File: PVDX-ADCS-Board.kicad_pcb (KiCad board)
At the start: 2 copper layers, 82.5 x 82.5 mm, 0 parts

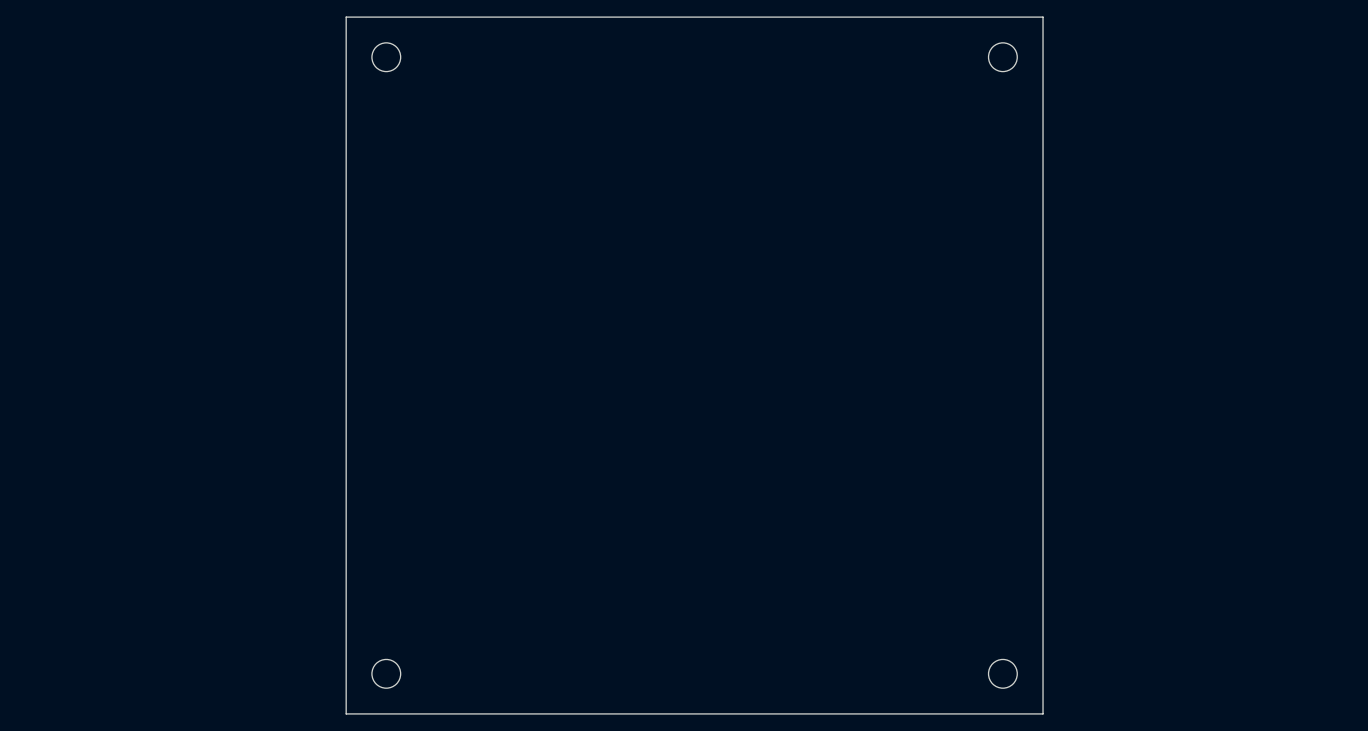
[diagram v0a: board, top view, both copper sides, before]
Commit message: routed PMB subcircuit, assigned eda models
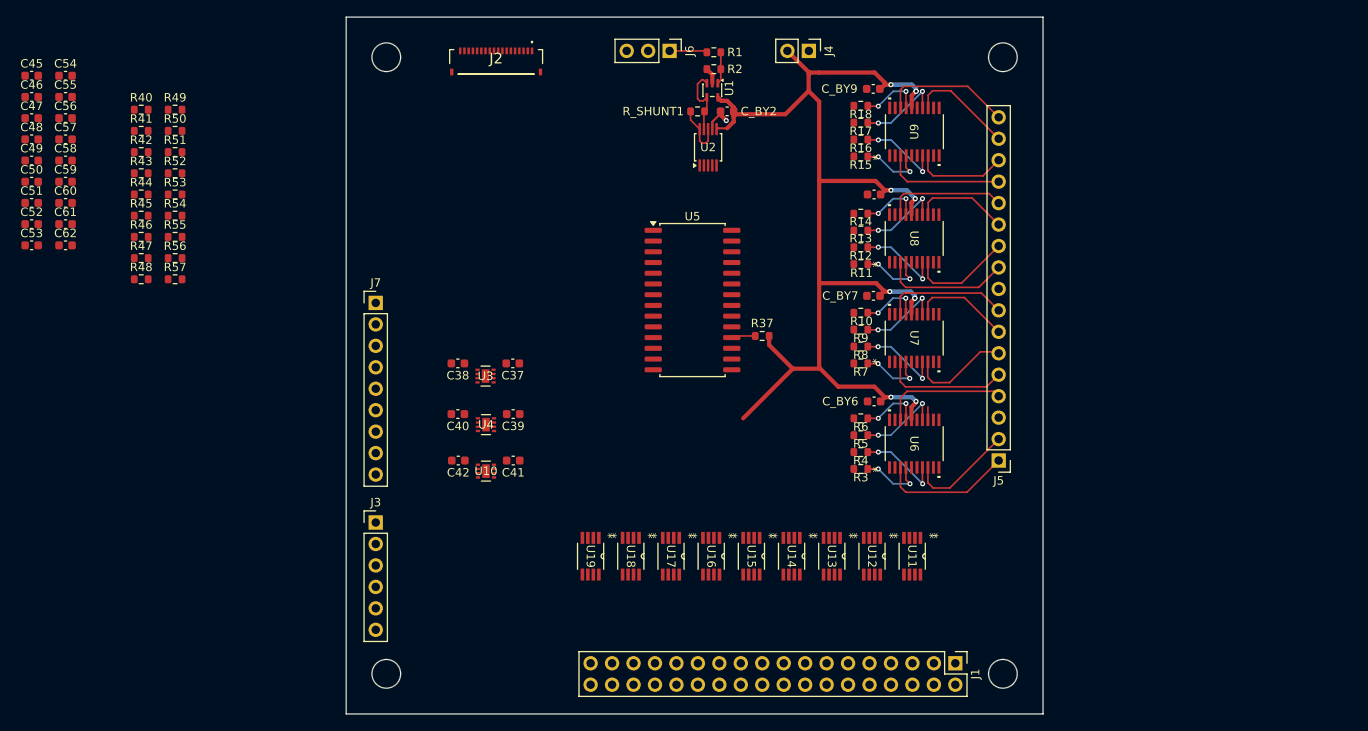
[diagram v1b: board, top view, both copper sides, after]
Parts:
- added C37: 0.1u, Capacitor_SMD:C_0603_1608Metric, F.Cu at (159.7, 78.5)
- added C38: 0.1u, Capacitor_SMD:C_0603_1608Metric, F.Cu at (153.2, 78.5)
- added C39: 0.1u, Capacitor_SMD:C_0603_1608Metric, F.Cu at (159.8, 84.5)
- added C40: 0.1u, Capacitor_SMD:C_0603_1608Metric, F.Cu at (153.2, 84.5)
- added C41: 0.1u, Capacitor_SMD:C_0603_1608Metric, F.Cu at (159.8, 90.0)
- added C42: 0.1u, Capacitor_SMD:C_0603_1608Metric, F.Cu at (153.3, 90.0)
- added C45: 22p, Capacitor_SMD:C_0603_1608Metric, F.Cu at (102.8, 44.4)
- added C46: 22p, Capacitor_SMD:C_0603_1608Metric, F.Cu at (102.8, 47.0)
- added C47: 22p, Capacitor_SMD:C_0603_1608Metric, F.Cu at (102.8, 49.5)
- added C48: 22p, Capacitor_SMD:C_0603_1608Metric, F.Cu at (102.8, 52.0)
- added C49: 22p, Capacitor_SMD:C_0603_1608Metric, F.Cu at (102.8, 54.5)
- added C50: 22p, Capacitor_SMD:C_0603_1608Metric, F.Cu at (102.8, 57.0)
- added C51: 22p, Capacitor_SMD:C_0603_1608Metric, F.Cu at (102.8, 59.5)
- added C52: 22p, Capacitor_SMD:C_0603_1608Metric, F.Cu at (102.8, 62.0)
- added C53: 22p, Capacitor_SMD:C_0603_1608Metric, F.Cu at (102.8, 64.5)
- added C54: 22p, Capacitor_SMD:C_0603_1608Metric, F.Cu at (106.8, 44.4)
- added C55: 22p, Capacitor_SMD:C_0603_1608Metric, F.Cu at (106.8, 47.0)
- added C56: 22p, Capacitor_SMD:C_0603_1608Metric, F.Cu at (106.8, 49.5)
- added C57: 22p, Capacitor_SMD:C_0603_1608Metric, F.Cu at (106.8, 52.0)
- added C58: 22p, Capacitor_SMD:C_0603_1608Metric, F.Cu at (106.8, 54.5)
- added C59: 22p, Capacitor_SMD:C_0603_1608Metric, F.Cu at (106.8, 57.0)
- added C60: 22p, Capacitor_SMD:C_0603_1608Metric, F.Cu at (106.8, 59.5)
- added C61: 22p, Capacitor_SMD:C_0603_1608Metric, F.Cu at (106.8, 62.0)
- added C62: 22p, Capacitor_SMD:C_0603_1608Metric, F.Cu at (106.8, 64.5)
- added C_BY2: 0.1u, Capacitor_SMD:C_0603_1608Metric, F.Cu at (185.1, 48.7)
- added C_BY6: 0.1u, Capacitor_SMD:C_0603_1608Metric, F.Cu at (202.5, 83.0)
- added C_BY7: 0.1u, Capacitor_SMD:C_0603_1608Metric, F.Cu at (202.4, 70.5)
- added C_BY8: 0.1u, Capacitor_SMD:C_0603_1608Metric, F.Cu at (202.5, 58.5)
- added C_BY9: 0.1u, Capacitor_SMD:C_0603_1608Metric, F.Cu at (202.4, 46.0)
- added J1: Conn_02x18_Row_Letter_Last, Connector_PinHeader_2.54mm:PinHeader_2x18_P2.54mm_Vertical, F.Cu at (212.1, 114.0)
- added J2: Conn_01x18, footprints:FH34SRJ18S05SH50, F.Cu at (157.8, 42.8)
- added J3: Conn_01x06, Connector_PinHeader_2.54mm:PinHeader_1x06_P2.54mm_Vertical, F.Cu at (143.5, 97.3)
- added J4: Conn_01x02, Connector_PinHeader_2.54mm:PinHeader_1x02_P2.54mm_Vertical, F.Cu at (194.8, 41.5)
- added J5: Conn_01x17, Connector_PinHeader_2.54mm:PinHeader_1x17_P2.54mm_Vertical, F.Cu at (217.2, 90.0)
- added J6: Conn_01x03, Connector_PinHeader_2.54mm:PinHeader_1x03_P2.54mm_Vertical, F.Cu at (178.3, 41.5)
- added J7: Conn_01x09, Connector_PinHeader_2.54mm:PinHeader_1x09_P2.54mm_Vertical, F.Cu at (143.5, 71.3)
- added R1: 21k, Resistor_SMD:R_0603_1608Metric, F.Cu at (183.5, 41.7)
- added R10: R_US, Resistor_SMD:R_0603_1608Metric, F.Cu at (200.9, 72.5)
- added R11: R_US, Resistor_SMD:R_0603_1608Metric, F.Cu at (200.9, 66.8)
- added R12: R_US, Resistor_SMD:R_0603_1608Metric, F.Cu at (200.9, 64.8)
- added R13: R_US, Resistor_SMD:R_0603_1608Metric, F.Cu at (200.9, 62.8)
- added R14: R_US, Resistor_SMD:R_0603_1608Metric, F.Cu at (200.9, 60.8)
- added R15: R_US, Resistor_SMD:R_0603_1608Metric, F.Cu at (200.9, 54.0)
- added R16: R_US, Resistor_SMD:R_0603_1608Metric, F.Cu at (200.9, 52.0)
- added R17: R_US, Resistor_SMD:R_0603_1608Metric, F.Cu at (200.9, 50.0)
- added R18: R_US, Resistor_SMD:R_0603_1608Metric, F.Cu at (200.9, 48.0)
- added R2: 12k, Resistor_SMD:R_0603_1608Metric, F.Cu at (183.5, 43.7)
- added R3: R_US, Resistor_SMD:R_0603_1608Metric, F.Cu at (200.9, 91.0)
- added R37: 10k, Resistor_SMD:R_0603_1608Metric, F.Cu at (189.2, 75.2)
- added R4: R_US, Resistor_SMD:R_0603_1608Metric, F.Cu at (200.9, 89.0)
- added R40: 2.2k, Resistor_SMD:R_0603_1608Metric, F.Cu at (115.7, 48.5)
- added R41: 2.2k, Resistor_SMD:R_0603_1608Metric, F.Cu at (115.7, 51.0)
- added R42: 2.2k, Resistor_SMD:R_0603_1608Metric, F.Cu at (115.7, 53.5)
- added R43: 2.2k, Resistor_SMD:R_0603_1608Metric, F.Cu at (115.7, 56.0)
- added R44: 2.2k, Resistor_SMD:R_0603_1608Metric, F.Cu at (115.7, 58.5)
- added R45: 2.2k, Resistor_SMD:R_0603_1608Metric, F.Cu at (115.7, 61.0)
- added R46: 2.2k, Resistor_SMD:R_0603_1608Metric, F.Cu at (115.7, 63.5)
- added R47: 2.2k, Resistor_SMD:R_0603_1608Metric, F.Cu at (115.7, 66.0)
- added R48: 2.2k, Resistor_SMD:R_0603_1608Metric, F.Cu at (115.7, 68.5)
- added R49: 2.2k, Resistor_SMD:R_0603_1608Metric, F.Cu at (119.7, 48.5)
- added R5: R_US, Resistor_SMD:R_0603_1608Metric, F.Cu at (200.9, 87.0)
- added R50: 2.2k, Resistor_SMD:R_0603_1608Metric, F.Cu at (119.7, 51.0)
- added R51: 2.2k, Resistor_SMD:R_0603_1608Metric, F.Cu at (119.7, 53.5)
- added R52: 2.2k, Resistor_SMD:R_0603_1608Metric, F.Cu at (119.7, 56.0)
- added R53: 2.2k, Resistor_SMD:R_0603_1608Metric, F.Cu at (119.7, 58.5)
- added R54: 2.2k, Resistor_SMD:R_0603_1608Metric, F.Cu at (119.7, 61.0)
- added R55: 2.2k, Resistor_SMD:R_0603_1608Metric, F.Cu at (119.7, 63.5)
- added R56: 2.2k, Resistor_SMD:R_0603_1608Metric, F.Cu at (119.7, 66.0)
- added R57: 2.2k, Resistor_SMD:R_0603_1608Metric, F.Cu at (119.7, 68.5)
- added R6: R_US, Resistor_SMD:R_0603_1608Metric, F.Cu at (200.9, 85.0)
- added R7: R_US, Resistor_SMD:R_0603_1608Metric, F.Cu at (200.9, 78.5)
- added R8: R_US, Resistor_SMD:R_0603_1608Metric, F.Cu at (200.9, 76.5)
- added R9: R_US, Resistor_SMD:R_0603_1608Metric, F.Cu at (200.9, 74.5)
- added R_SHUNT1: 10, Resistor_SMD:R_0603_1608Metric, F.Cu at (181.6, 48.7)
- added U1: TLV9001IDCK, Package_TO_SOT_SMD:SOT-353_SC-70-5, F.Cu at (183.3, 46.2)
- added U10: DRV8837C, footprints:DSG8_P9X1P6_TEX, F.Cu at (156.5, 91.2)
- added U11: OPA2381AIDGKR, footprints:DGK8, F.Cu at (207.0, 101.3)
- added U12: OPA2381AIDGKR, footprints:DGK8, F.Cu at (202.3, 101.3)
- added U13: OPA2381AIDGKR, footprints:DGK8, F.Cu at (197.5, 101.3)
- added U14: OPA2381AIDGKR, footprints:DGK8, F.Cu at (192.7, 101.3)
- added U15: OPA2381AIDGKR, footprints:DGK8, F.Cu at (188.0, 101.3)
- added U16: OPA2381AIDGKR, footprints:DGK8, F.Cu at (183.2, 101.3)
- added U17: OPA2381AIDGKR, footprints:DGK8, F.Cu at (178.5, 101.3)
- added U18: OPA2381AIDGKR, footprints:DGK8, F.Cu at (173.7, 101.3)
- added U19: OPA2381AIDGKR, footprints:DGK8, F.Cu at (168.9, 101.3)
- added U2: INA226, Package_SO:TSSOP-10_3x3mm_P0.5mm, F.Cu at (182.8, 52.9)
- added U3: DRV8837C, footprints:DSG8_P9X1P6_TEX, F.Cu at (156.5, 80.0)
- added U4: DRV8837C, footprints:DSG8_P9X1P6_TEX, F.Cu at (156.5, 85.8)
- added U5: MCP23017x-x-SO, Package_SO:SOIC-28W_7.5x17.9mm_P1.27mm, F.Cu at (181.0, 71.0)
- added U6: ADG734BRUZ, footprints:RU_20_ADI, F.Cu at (207.2, 88.0)
- added U7: ADG734BRUZ, footprints:RU_20_ADI, F.Cu at (207.2, 75.5)
- added U8: ADG734BRUZ, footprints:RU_20_ADI, F.Cu at (207.3, 63.7)
- added U9: ADG734BRUZ, footprints:RU_20_ADI, F.Cu at (207.3, 51.1)
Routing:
- net +3V3: track 0.00 -> 135.4 mm, vias 0 -> 10
- net PIXEL1+: track 0.00 -> 15.7 mm
- net PIXEL16+: track 0.00 -> 15.4 mm
- net PIXEL9+: track 0.00 -> 15.2 mm
- net PIXEL5+: track 0.00 -> 14.8 mm
- net PIXEL8+: track 0.00 -> 14.8 mm
- net PIXEL4+: track 0.00 -> 14.8 mm
- net PIXEL12+: track 0.00 -> 14.4 mm
- net PIXEL13+: track 0.00 -> 14.3 mm
- net PIXEL2+: track 0.00 -> 12.8 mm
- net PIXEL15+: track 0.00 -> 12.4 mm
- net PIXEL10+: track 0.00 -> 12.3 mm
- net PIXEL6+: track 0.00 -> 12.0 mm
- net PIXEL7+: track 0.00 -> 11.7 mm
- net PIXEL11+: track 0.00 -> 11.3 mm
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
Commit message: finished PMB layout, 50% MTQ layout
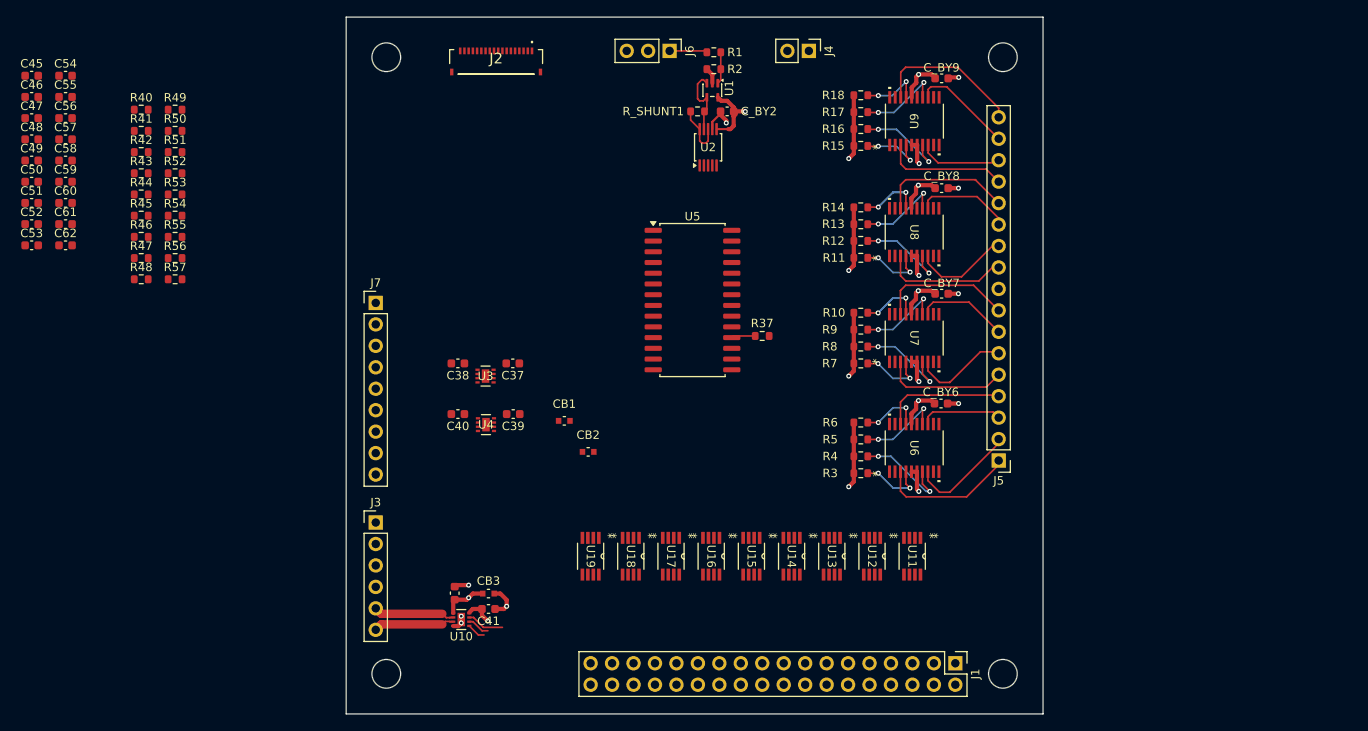
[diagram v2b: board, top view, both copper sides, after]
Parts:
- added CB1: 22u, footprints:GRM18x, F.Cu at (165.8, 85.3)
- added CB2: 22u, footprints:GRM18x, F.Cu at (168.7, 89.0)
- added CB3: 22u, footprints:GRM18x, F.Cu at (156.8, 105.8)
- R10, R11, R12, R13, R14, R15, R16, R17, R18, R3, R4, R5, R6, R7, R8, R9: value R_US -> 100
- moved C41 17.8 mm to (156.8, 107.6)
- moved U10 17.8 mm to (153.6, 108.8)
- moved C42 15.7 mm to (152.8, 105.7), turned to 90 degrees
- moved C_BY9 8.20 mm to (210.5, 44.8), turned to 180 degrees
- moved C_BY7 8.08 mm to (210.5, 70.2), turned to 0 degrees
- moved C_BY8 8.04 mm to (210.5, 57.8), turned to 0 degrees
- moved C_BY6 7.93 mm to (210.4, 83.2), turned to 0 degrees
- moved R15 1.25 mm to (200.9, 52.8)
- moved R16 1.25 mm to (200.9, 50.8)
- moved R17 1.25 mm to (200.9, 48.8)
- moved R18 1.25 mm to (200.9, 46.8)
- moved U9 1.25 mm to (207.3, 49.8)
- moved R11 0.75 mm to (200.9, 66.0)
- moved R12 0.75 mm to (200.9, 64.0)
- moved R13 0.75 mm to (200.9, 62.0)
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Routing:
- net +3V3: track 135.4 -> 37.5 mm, vias 10 -> 7
- net GND: track 5.80 -> 62.3 mm, vias 1 -> 17
- net MTQ3+: track 0.00 -> 9.64 mm
- net MTQ3-: track 0.00 -> 9.60 mm
- net PIXEL3+: track 1.56 -> 9.75 mm
- net MSLEEP3: track 0.00 -> 4.41 mm
- net Net-(U8-S4B): track 7.31 -> 11.3 mm
- net Net-(U7-S4B): track 7.31 -> 11.3 mm
- net MCTRL3_1: track 0.00 -> 2.65 mm
- net PIXEL16+: track 15.4 -> 17.9 mm
- net MCTRL3_2: track 0.00 -> 2.19 mm
- net Net-(U7-S2B): track 10.0 -> 11.8 mm
- net Net-(U6-S2B): track 10.0 -> 11.8 mm
- net PIXEL12+: track 14.4 -> 15.8 mm
- net PIXEL14+: track 11.2 -> 9.90 mm
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- added copper zone on In2.Cu, net +3V3
- added copper zone on In1.Cu, net GND
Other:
- copper layers 2 -> 4

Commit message: placed MTQ drivers
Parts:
- moved C39 18.2 mm to (156.8, 102.5)
- moved U4 18.2 mm to (153.6, 103.8)
- moved C37 16.8 mm to (156.8, 95.1)
- moved CB2 16.6 mm to (156.8, 100.7)
- moved U3 16.6 mm to (153.6, 96.3)
- moved C40 16.1 mm to (152.8, 100.6), turned to 90 degrees
- moved C38 14.7 mm to (152.8, 93.2), turned to 90 degrees
- moved CB1 12.0 mm to (156.8, 93.2)
- moved C41 3.00 mm to (156.8, 110.6)
- moved C42 3.00 mm to (152.8, 108.7)
- moved CB3 3.00 mm to (156.8, 108.8)
- moved U10 3.00 mm to (153.6, 111.8)
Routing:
- net +3V3: track 37.5 -> 54.8 mm, vias 7 -> 11
- net GND: track 62.3 -> 77.7 mm, vias 17 -> 25
- net MTQ1+: track 0.00 -> 10.6 mm
- net MTQ1-: track 0.00 -> 10.6 mm
- net MTQ2+: track 0.00 -> 9.48 mm
- net MTQ2-: track 0.00 -> 9.43 mm
- net MSLEEP3: track 4.41 -> 0.00 mm
- net MCTRL3_1: track 2.65 -> 0.00 mm
- net MCTRL3_2: track 2.19 -> 0.00 mm
- net MTQ3+: track 9.64 -> 10.9 mm
- net MTQ3-: track 9.60 -> 10.3 mm

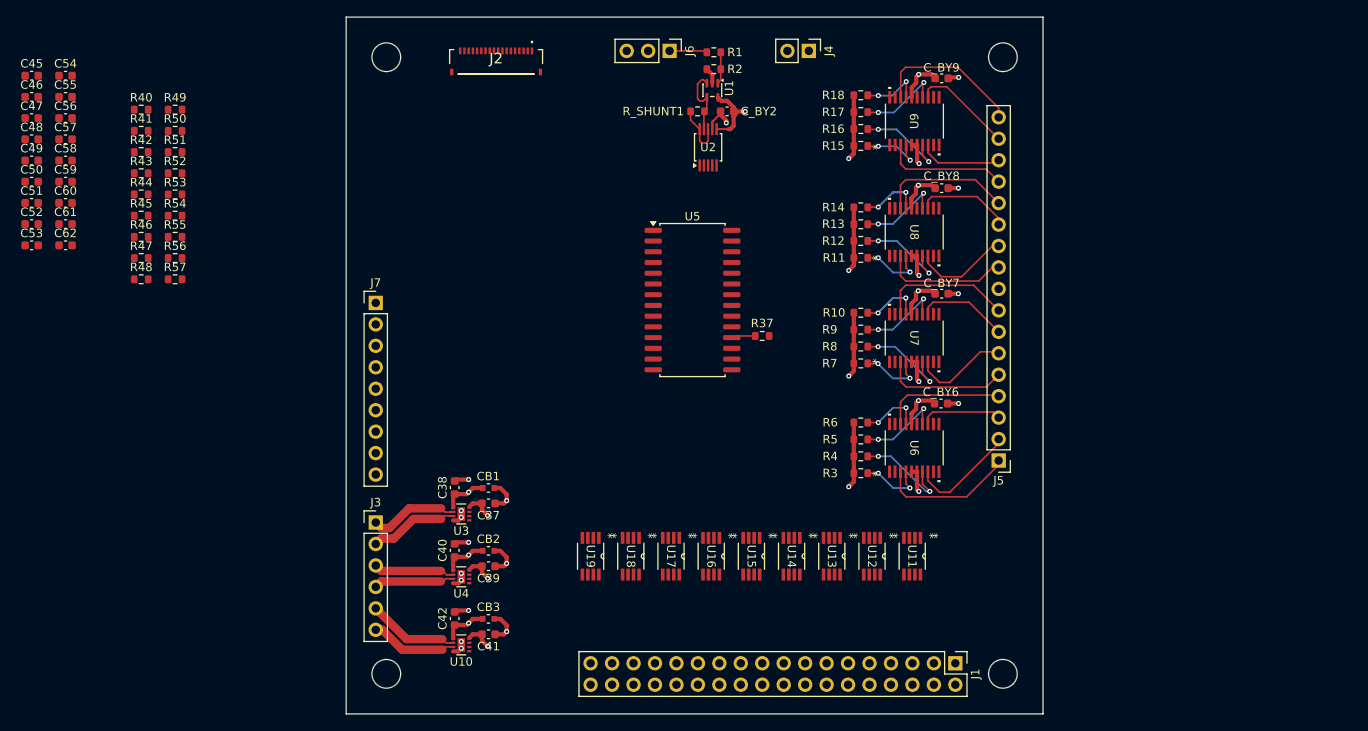
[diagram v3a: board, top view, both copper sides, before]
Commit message: 50% PD, 80% MTQ, 90% PMB layout
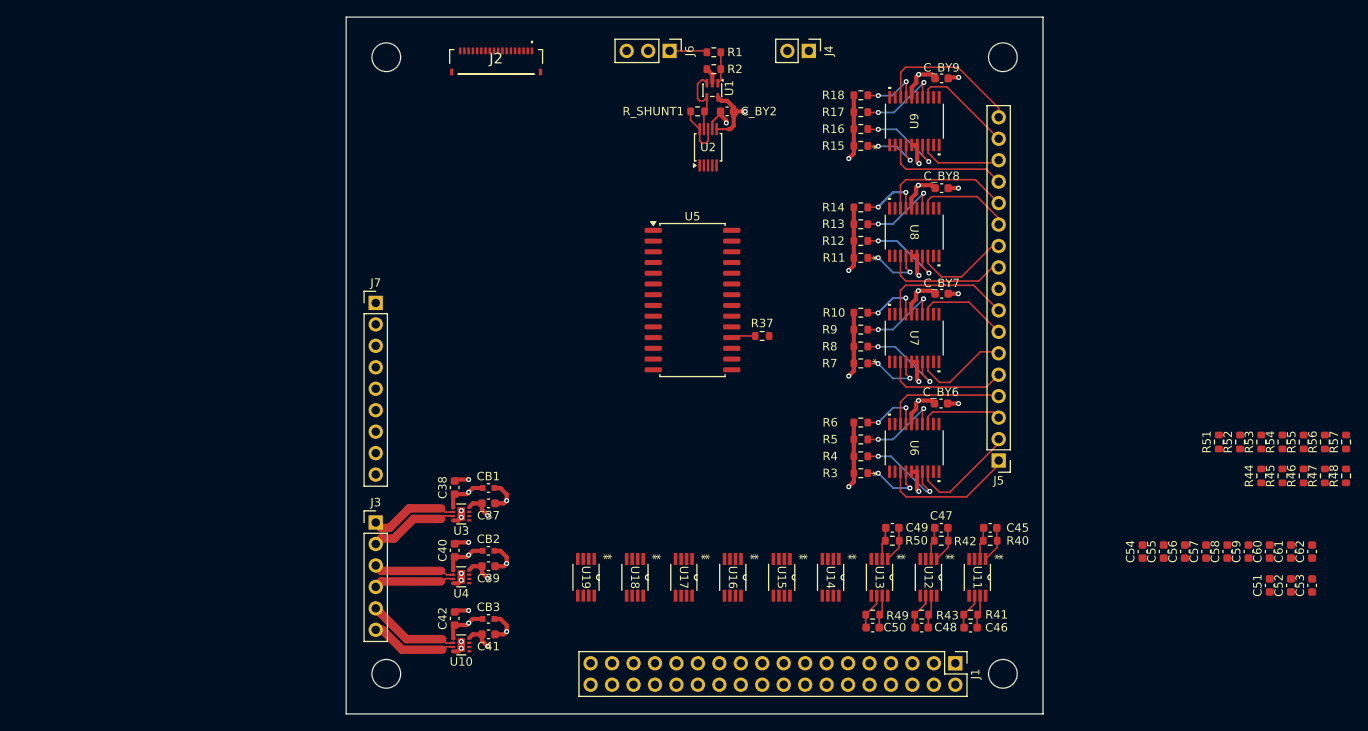
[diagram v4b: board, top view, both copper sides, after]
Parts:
- moved C53 156.9 mm to (254.4, 104.8), turned to 90 degrees
- moved C52 155.1 mm to (251.8, 104.8), turned to 90 degrees
- moved C51 153.4 mm to (249.3, 104.8), turned to 90 degrees
- moved C62 152.0 mm to (254.4, 100.8), turned to 90 degrees
- moved C61 150.2 mm to (251.8, 100.8), turned to 90 degrees
- moved C60 148.4 mm to (249.3, 100.8), turned to 90 degrees
- moved C59 146.7 mm to (246.8, 100.8), turned to 90 degrees
- moved C58 145.1 mm to (244.3, 100.8), turned to 90 degrees
- moved R48 144.5 mm to (258.4, 91.8), turned to 90 degrees
- moved C57 143.6 mm to (241.8, 100.8), turned to 90 degrees
- moved R47 142.5 mm to (255.9, 91.8), turned to 90 degrees
- moved C56 142.1 mm to (239.3, 100.8), turned to 90 degrees
- moved C55 140.7 mm to (236.8, 100.8), turned to 90 degrees
- moved R46 140.5 mm to (253.4, 91.8), turned to 90 degrees
- moved R57 140.0 mm to (258.4, 87.8), turned to 90 degrees
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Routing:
- net PD2: track 0.00 -> 8.68 mm
- net PD1_OUT: track 0.00 -> 8.55 mm
- net PD2_OUT: track 0.00 -> 7.85 mm
- net PD1: track 0.00 -> 7.73 mm
- net PD4: track 0.00 -> 4.34 mm
- net PD3_OUT: track 0.00 -> 4.28 mm
- net PD4_OUT: track 0.00 -> 3.92 mm
- net PD3: track 0.00 -> 3.86 mm
